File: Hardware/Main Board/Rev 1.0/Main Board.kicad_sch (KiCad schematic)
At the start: 56 parts, among them J1 PWR_SW, J10 6502 Bus, J2 Conn_02x01, J3 USB_C_Receptacle_USB2.0, J4 RESET_SW, J5 Conn_02x02_Odd_Even, J6 CLOCK_ENBL_SW, J7 Conn_01x02, J8 Conn_02x05_Odd_Even, J9 6502 Card Connector, Q1 SS8050, SW1 Reset, U1 LM555xM, U2 AS6C62256, U3 AT28C256, U4 74HC00, U5 74HC00, U6 65C02, U7 74HC00, X1 OCXO-14

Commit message: Add BOMs
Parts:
- J1, J10, J2, J4, J5, J6, J7, J8, JP1, JP2, JP3, JP4, JP5, JP6, U2, U3, U6, X1: now in the parts list
- J9: Digikey (none) -> A31723-ND; now in the parts list
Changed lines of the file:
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@@
 			)
 		)
-		(property "Sim.Pins" "1=K 2=A"
-			(at 87.63 35.56 0)
-			(hide yes)
-			(show_name no)
-			(do_not_autoplace no)
-			(effects
-				(font
-					(size 1.27 1.27)
-				)
-			)
-		)
 		(pin "1"
 		)
@@
 		(body_style 1)
 		(exclude_from_sim no)
-		(in_bom no)
+		(in_bom yes)
 		(on_board yes)
 		(in_pos_files yes)
@@
 		(body_style 1)
 		(exclude_from_sim no)
-		(in_bom no)
+		(in_bom yes)
 		(on_board yes)
 		(in_pos_files yes)
@@
 		(body_style 1)
 		(exclude_from_sim no)
-		(in_bom no)
+		(in_bom yes)
 		(on_board yes)
 		(in_pos_files yes)
@@
 			)
 		)
+		(property "Digikey" "A31723-ND"
+			(at 39.37 219.71 0)
+			(hide yes)
+			(show_name no)
+			(do_not_autoplace no)
+			(effects
+				(font
+					(size 1.27 1.27)
+				)
+			)
+		)
 		(pin "1"
 		)
@@
 		(body_style 1)
 		(exclude_from_sim no)
-		(in_bom no)
+		(in_bom yes)
 		(on_board yes)
 		(in_pos_files yes)
@@
 		(body_style 1)
 		(exclude_from_sim no)
-		(in_bom no)
+		(in_bom yes)
 		(on_board yes)
 		(in_pos_files yes)
@@
 		(body_style 1)
 		(exclude_from_sim no)
-		(in_bom no)
+		(in_bom yes)
 		(on_board yes)
 		(in_pos_files yes)
@@
 		(body_style 1)
 		(exclude_from_sim no)
-		(in_bom no)
+		(in_bom yes)
 		(on_board yes)
 		(in_pos_files yes)
@@
 			)
 		)
-		(property "Description" ""
+		(property "Description" "Unpolarized capacitor"
 			(at 223.52 208.28 0)
 			(hide yes)
@@
 		(body_style 1)
 		(exclude_from_sim no)
-		(in_bom no)
+		(in_bom yes)
 		(on_board yes)
 		(in_pos_files yes)
@@
 		(body_style 1)
 		(exclude_from_sim no)
-		(in_bom no)
+		(in_bom yes)
 		(on_board yes)
 		(in_pos_files yes)
@@
 		(body_style 1)
 		(exclude_from_sim no)
-		(in_bom no)
+		(in_bom yes)
 		(on_board yes)
 		(in_pos_files yes)
@@
 		(body_style 1)
 		(exclude_from_sim no)
-		(in_bom no)
+		(in_bom yes)
 		(on_board yes)
 		(in_pos_files yes)
@@
 		(body_style 1)
 		(exclude_from_sim no)
-		(in_bom no)
+		(in_bom yes)
 		(on_board yes)
 		(in_pos_files yes)
@@
 			)
 		)
-		(property "Description" ""
+		(property "Description" "Unpolarized capacitor"
 			(at 246.38 208.28 0)
 			(hide yes)
@@
 		(body_style 1)
 		(exclude_from_sim no)
-		(in_bom no)
+		(in_bom yes)
 		(on_board yes)
 		(in_pos_files yes)
@@
 		(body_style 1)
 		(exclude_from_sim no)
-		(in_bom no)
+		(in_bom yes)
 		(on_board yes)
 		(in_pos_files yes)
@@
 			)
 		)
-		(property "Description" ""
+		(property "Description" "Unpolarized capacitor"
 			(at 311.15 93.98 0)
 			(hide yes)
@@
 		(body_style 1)
 		(exclude_from_sim no)
-		(in_bom no)
+		(in_bom yes)
 		(on_board yes)
 		(in_pos_files yes)
@@
 		(body_style 1)
 		(exclude_from_sim no)
-		(in_bom no)
+		(in_bom yes)
 		(on_board yes)
 		(in_pos_files yes)
@@
 		(body_style 1)
 		(exclude_from_sim no)
-		(in_bom no)
+		(in_bom yes)
 		(on_board yes)
 		(in_pos_files yes)
@@
 		(body_style 1)
 		(exclude_from_sim no)
-		(in_bom no)
+		(in_bom yes)
 		(on_board yes)
 		(in_pos_files yes)
@@
 			)
 		)
-		(property "Description" ""
+		(property "Description" "Unpolarized capacitor"
 			(at 369.57 93.98 0)
 			(hide yes)
@@
 			)
 		)
-		(property "Description" ""
+		(property "Description" "Unpolarized capacitor"
 			(at 199.39 208.28 0)
 			(hide yes)
@@
 		(body_style 1)
 		(exclude_from_sim no)
-		(in_bom no)
+		(in_bom yes)
 		(on_board yes)
 		(in_pos_files yes)

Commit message: Finish BOM and add to README
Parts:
- J10: Other (none) -> https://www.amazon.com/Female-Headers-Connector-Header-Rasp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
- J2: value Conn_02x01 -> ROM WE; Other (none) -> https://www.amazon.com/Straight-Breakaway-Connector-Breadbo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
- J5: value Conn_02x02_Odd_Even -> HRDB EN; Other (none) -> https://www.amazon.com/Uxcell-Double-Straight-Header-Strip/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
- J7: value Conn_01x02 -> 6502 EN; Other (none) -> https://www.amazon.com/Straight-Breakaway-Connector-Breadbo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
- J8: value Conn_02x05_Odd_Even -> EXP EN; Other (none) -> https://www.amazon.com/Uxcell-Double-Straight-Header-Strip/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
- JP1, JP2, JP3, JP4, JP5, JP6: now left out of the parts list
- U2: Digikey (none) -> 1450-1033-ND; Mouser (none) -> 913-AS6C62256-55PCN
- U3: Digikey (none) -> AT28C256-15PU-ND; Mouser (none) -> 556-AT28C25615PU
- U6: Mouser (none) -> 955-W65C02S6TPG-14
- X1: Digikey (none) -> X937-ND

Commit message: Restore exclude from BOM
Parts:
- J1, J10, J2, J4, J5, J6, J7, J8, J9, U2, U3, U6, X1: now left out of the parts list
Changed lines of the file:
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@@
 		(body_style 1)
 		(exclude_from_sim no)
-		(in_bom yes)
+		(in_bom no)
 		(on_board yes)
 		(in_pos_files yes)
@@
 		(body_style 1)
 		(exclude_from_sim no)
-		(in_bom yes)
+		(in_bom no)
 		(on_board yes)
 		(in_pos_files yes)
@@
 		(body_style 1)
 		(exclude_from_sim no)
-		(in_bom yes)
+		(in_bom no)
 		(on_board yes)
 		(in_pos_files yes)
@@
 		(body_style 1)
 		(exclude_from_sim no)
-		(in_bom yes)
+		(in_bom no)
 		(on_board yes)
 		(in_pos_files yes)
@@
 		(body_style 1)
 		(exclude_from_sim no)
-		(in_bom yes)
+		(in_bom no)
 		(on_board yes)
 		(in_pos_files yes)
@@
 		(body_style 1)
 		(exclude_from_sim no)
-		(in_bom yes)
+		(in_bom no)
 		(on_board yes)
 		(in_pos_files yes)
@@
 		(body_style 1)
 		(exclude_from_sim no)
-		(in_bom yes)
+		(in_bom no)
 		(on_board yes)
 		(in_pos_files yes)
@@
 		(body_style 1)
 		(exclude_from_sim no)
-		(in_bom yes)
+		(in_bom no)
 		(on_board yes)
 		(in_pos_files yes)
@@
 		(body_style 1)
 		(exclude_from_sim no)
-		(in_bom yes)
+		(in_bom no)
 		(on_board yes)
 		(in_pos_files yes)
@@
 		(body_style 1)
 		(exclude_from_sim no)
-		(in_bom yes)
+		(in_bom no)
 		(on_board yes)
 		(in_pos_files yes)
@@
 		(body_style 1)
 		(exclude_from_sim no)
-		(in_bom yes)
+		(in_bom no)
 		(on_board yes)
 		(in_pos_files yes)
@@
 		(body_style 1)
 		(exclude_from_sim no)
-		(in_bom yes)
+		(in_bom no)
 		(on_board yes)
 		(in_pos_files yes)
@@
 		(body_style 1)
 		(exclude_from_sim no)
-		(in_bom yes)
+		(in_bom no)
 		(on_board yes)
 		(in_pos_files yes)

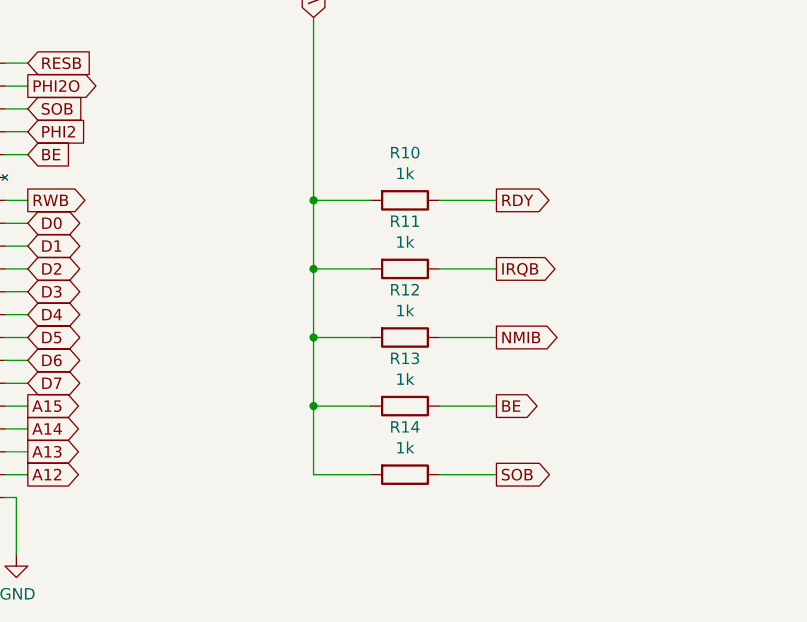
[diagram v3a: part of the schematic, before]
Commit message: Change pull up resistor values
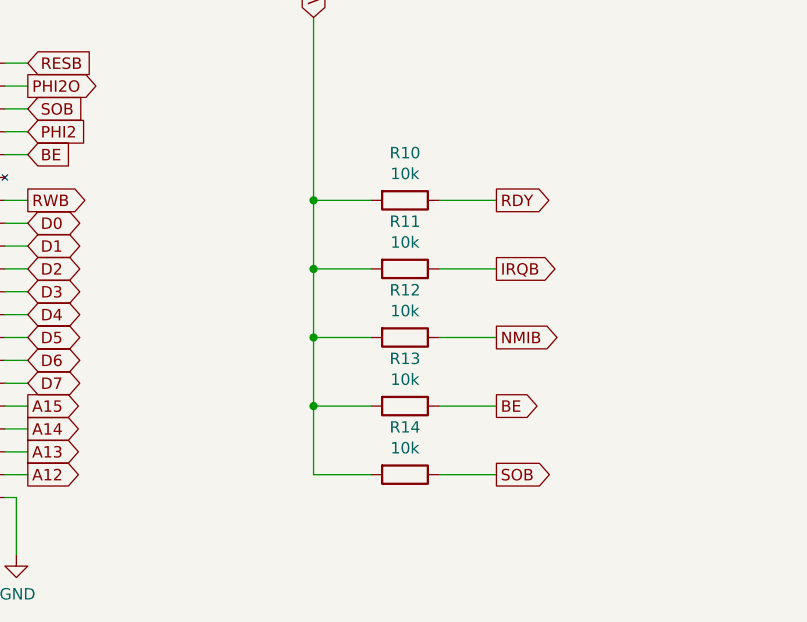
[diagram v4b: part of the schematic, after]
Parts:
- R10, R11, R12, R13, R14: value 1k -> 10k; LCSC C17513 -> C2930231
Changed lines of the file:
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@@
 			)
 		)
-		(property "Value" "1k"
+		(property "Value" "10k"
 			(at 372.11 134.2136 90)
 			(show_name no)
@@
 			)
 		)
-		(property "LCSC" "C17513"
+		(property "LCSC" "C2930231"
 			(at 372.11 137.16 0)
 			(hide yes)
@@
 			)
 		)
-		(property "Value" "1k"
+		(property "Value" "10k"
 			(at 372.11 149.4536 90)
 			(show_name no)
@@
 			)
 		)
-		(property "LCSC" "C17513"
+		(property "LCSC" "C2930231"
 			(at 372.11 152.4 0)
 			(hide yes)
@@
 			)
 		)
-		(property "Value" "1k"
+		(property "Value" "10k"
 			(at 372.11 141.8336 90)
 			(show_name no)
@@
 			)
 		)
-		(property "LCSC" "C17513"
+		(property "LCSC" "C2930231"
 			(at 372.11 144.78 0)
 			(hide yes)
@@
 			)
 		)
-		(property "Value" "1k"
+		(property "Value" "10k"
 			(at 372.11 164.6936 90)
 			(show_name no)
@@
 			)
 		)
-		(property "LCSC" "C17513"
+		(property "LCSC" "C2930231"
 			(at 372.11 167.64 0)
 			(hide yes)
@@
 			)
 		)
-		(property "Value" "1k"
+		(property "Value" "10k"
 			(at 372.11 157.0736 90)
 			(show_name no)
@@
 			)
 		)
-		(property "LCSC" "C17513"
+		(property "LCSC" "C2930231"
 			(at 372.11 160.02 0)
 			(hide yes)
